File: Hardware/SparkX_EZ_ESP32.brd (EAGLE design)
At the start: 10.7 x 40.6 mm, 59 parts, among them Q1 MBT3904DW1T1, U1 3.3V, U2 ESP32, U3 W25QXX128MBIT-6X5, U4 CP210X, X1 32.768kHz, X2 40MHz

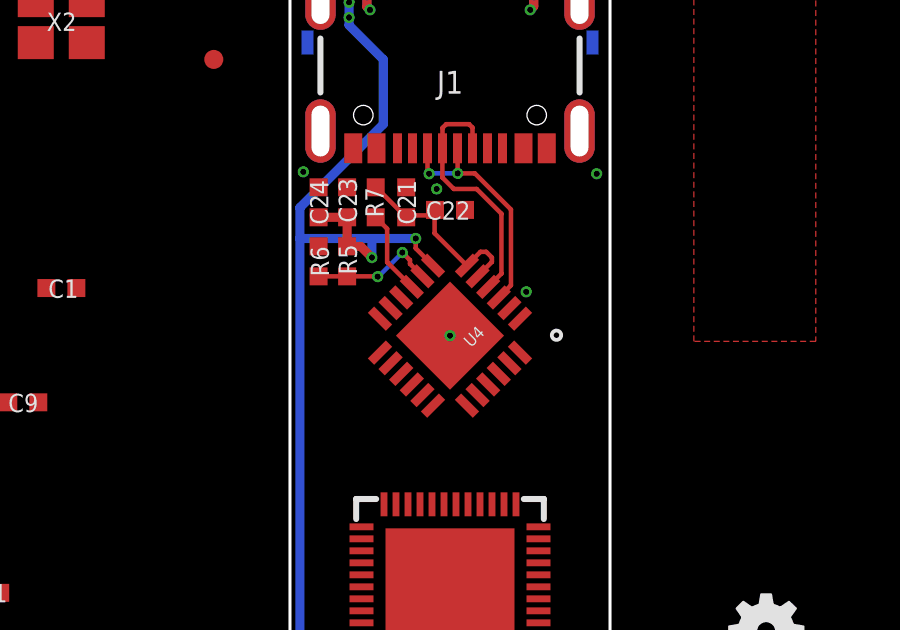
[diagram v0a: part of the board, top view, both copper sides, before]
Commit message: Add CP2102 package outline
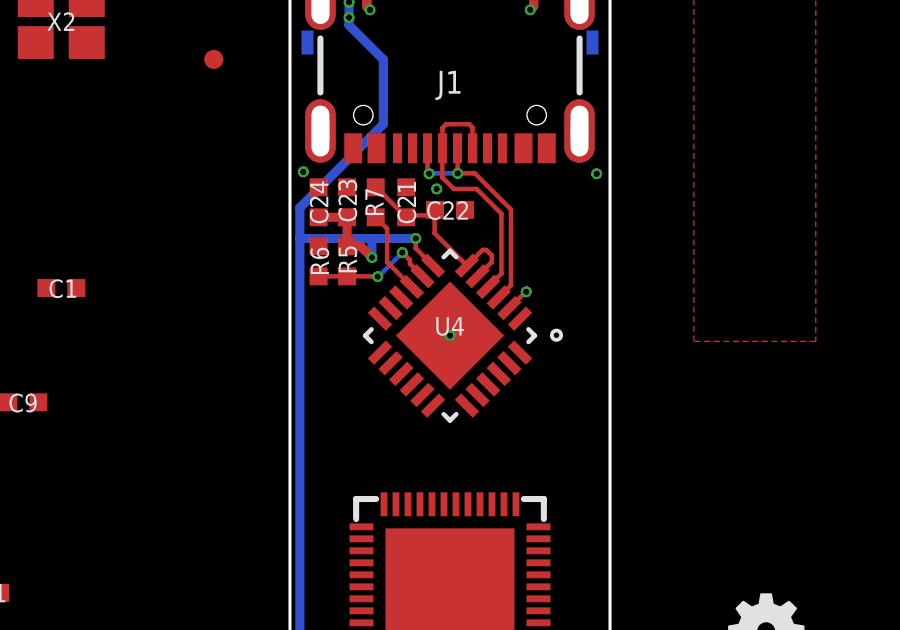
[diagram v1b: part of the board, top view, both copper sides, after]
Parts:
- A1: value (none) -> ANTENNA2.4GHZ-8.0X1.0MM
- U3: device SparkFun-MicroMod:WSON-8-6X5 -> SparkFun-IC-Memory:WSON-8-6X5
- U4: value CP210X -> CP2102N
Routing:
- net GND: track 7.88 -> 8.67 mm

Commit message: Routed
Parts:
- added !BOOT!, !RESET!, FLASH_VDD, RXT, TXT, USB_3V3: TEST-POINT3X4, SparkFun-Connectors:PAD.03X.04
- added U$10: (no value), output:#FVDD#0
- added U$2, U$3: (no value), output:EZ_ESP320
- added U$5: (no value), output:#TXT#0
- added U$6: (no value), output:#RXT#0
- added U$7: (no value), output:##BOOT##0
- added U$8: (no value), output:##RESET##0
- added U$9: (no value), output:#USB_3V3#0
- U3: value W25QXX128MBIT-6X5 -> W25QXX128MBIT-6X5-SKINNY_CENTER; device SparkFun-IC-Memory:WSON-8-6X5 -> SparkFun-IC-Memory:WSON-8-6X5-SKINNY_CENTERPAD
- moved U1 44.2 mm to (2.86, 5.14), flipped to the bottom, turned to 90 degrees
- moved C3 37.1 mm to (4.70, 19.4), flipped to the bottom, turned to 90 degrees
- moved Q1 35.8 mm to (6.35, 25.4), flipped to the bottom, turned to 270 degrees
- moved R10 35.4 mm to (8.64, 31.5), turned to 180 degrees
- moved C13 34.3 mm to (7.62, 23.9)
- moved C4 34.1 mm to (4.70, 17.4), flipped to the bottom, turned to 270 degrees
- moved C6 31.5 mm to (2.32, 22.5), turned to 270 degrees
- moved R1 31.2 mm to (1.78, 7.30), flipped to the bottom
- moved C7 30.4 mm to (2.32, 24.6), flipped to the bottom, turned to 270 degrees
- moved C15 30.0 mm to (9.81, 23.2), flipped to the bottom, turned to 90 degrees
- moved C2 29.4 mm to (5.40, 5.14), flipped to the bottom, turned to 90 degrees
- moved C1 27.8 mm to (1.78, 3.05), flipped to the bottom, turned to 180 degrees
- moved L1 26.2 mm to (2.32, 24.4), turned to 90 degrees
- moved R8 25.6 mm to (6.35, 27.2), flipped to the bottom
- moved R4 25.5 mm to (7.62, 23.0), turned to 180 degrees
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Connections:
- net 39-BATT/3 renamed N$3
- new net RXT: RXT.1, U4.13
- new net TXT: TXT.1, U4.14
- net !RESET: now also !RESET!.1
- net 0-!BOOT!: now also !BOOT!.1
- net FLASH_VDD: now also FLASH_VDD.1
- net USB_3V3: now also USB_3V3.1
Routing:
- net 3.3V: track 21.7 -> 125.6 mm, vias 6 -> 19
- net GND: track 8.67 -> 51.8 mm, vias 13 -> 47
- net SDA: track 41.7 -> 69.7 mm, vias 2 -> 3
- net SCL: track 41.5 -> 68.5 mm, vias 2 -> 3
- net 0-!BOOT!: track 0.00 -> 19.0 mm, vias 0 -> 2
- net CS1: track 42.0 -> 60.2 mm, vias 2 -> 3
- net FLASH_SDO: track 0.00 -> 14.9 mm
- net V_USB: track 53.2 -> 67.0 mm
- net FLASH_SCS: track 0.00 -> 13.1 mm
- net !RESET: track 0.00 -> 12.3 mm, vias 0 -> 1
- net PROC_PWR_EN: track 41.5 -> 53.6 mm, vias 2 -> 4
- net FLASH_SWP: track 0.00 -> 10.3 mm, vias 0 -> 2
- net FLASH_VDD: track 0.00 -> 9.47 mm, vias 0 -> 1
- net N$2: track 0.00 -> 9.26 mm, vias 0 -> 2
- net U0RXD: track 0.00 -> 9.14 mm
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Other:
- board text added: "JLCPCB JLC7628 4-Layer 1.6mm Impedance Control 4-Layer Board 1.6mm Thickness 1oz Copper (Outer layers) ENIG Finish When running the panelizer, add a vertical gap of 0.2" to make the boards easier to separate"
- board text removed: "JLCPCB JLC7628 4-Layer 0.8mm Impedance Control 4-Layer Board 0.8mm Thickness 1oz Copper (Outer layers) ENIG Finish When running the panelizer, add a vertical gap of 0.2" to make the boards easier to separate"

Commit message: Ready for review
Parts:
- moved C10 0.90 mm to (2.32, 23.4), turned to 270 degrees
- moved C7 0.89 mm to (2.32, 25.5), turned to 90 degrees
- moved C11 0.74 mm to (1.33, 21.3), turned to 270 degrees
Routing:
- net GND: track 51.8 -> 41.9 mm
- net 3: track 4.01 -> 2.72 mm
- net N$3: track 3.12 -> 2.02 mm
- net 6: track 3.41 -> 4.50 mm
- net RXT: track 3.79 -> 2.81 mm
- net V_USB: track 67.0 -> 67.8 mm
- net N$54: track 5.79 -> 5.26 mm

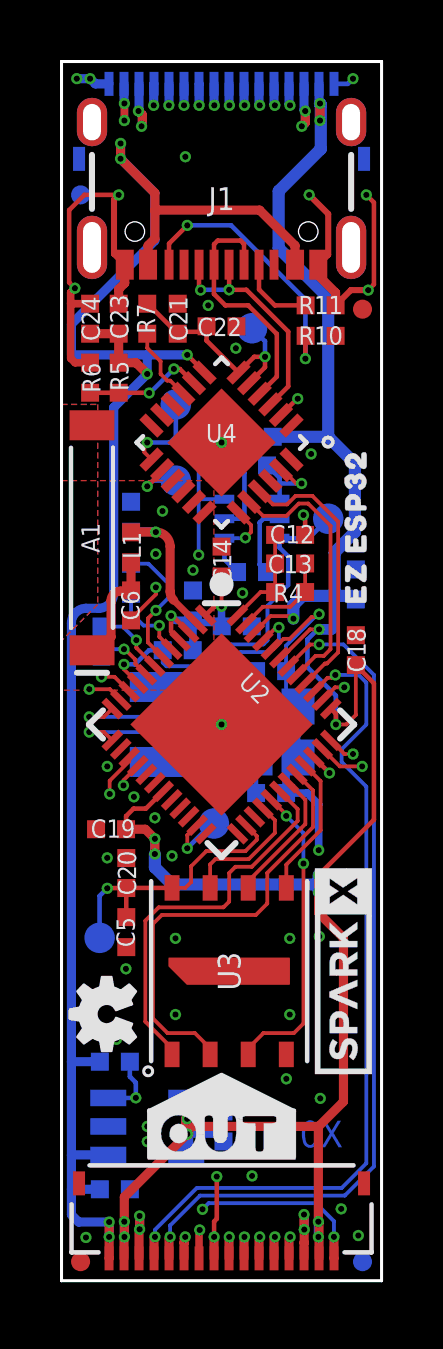
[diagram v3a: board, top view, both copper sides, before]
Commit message: Add neopixel. Add mirror-symmetric production panel
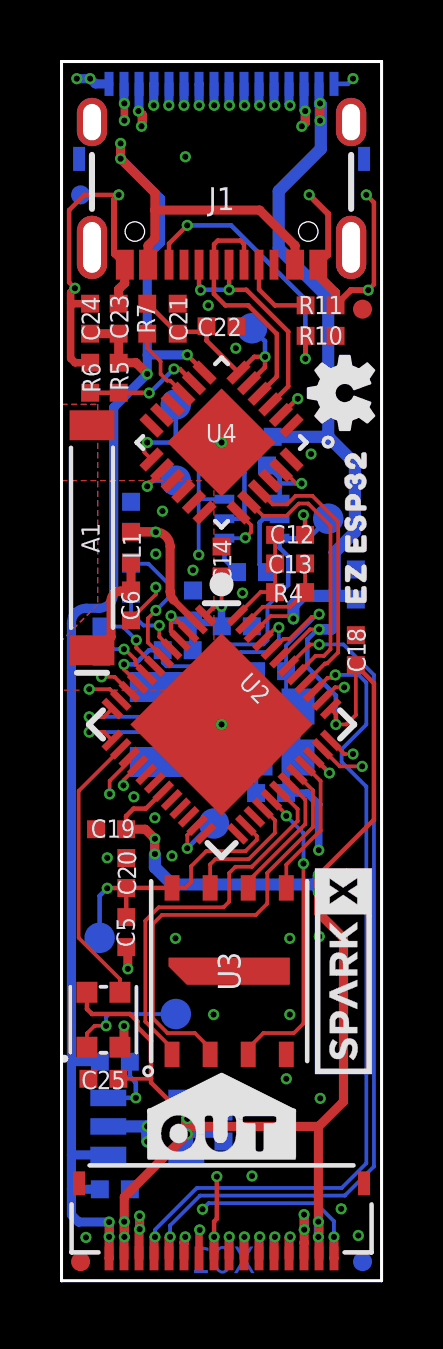
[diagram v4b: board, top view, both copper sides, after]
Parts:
- added C25: 0.1uF, SparkFun-Capacitors:0402-TIGHT
- added D1: WS2812_2020, SparkFun-LED:WS2812-2020
- added LED_DO: TEST-POINT3X4, SparkFun-Connectors:PAD.03X.04
- added LOGO4: SPECIAL_INSTRUCTIONS-PRODUCTION, SparkFun-Aesthetics:PRODUCTION_INSTRUCTIONS
- added U$11: (no value), output:#LED_DO#0
- U1: value 3.3V -> MIC5219 3.3V
- moved FRAME1 31.9 mm to (48.3, -41.9)
- moved LOGO2 22.2 mm to (9.43, 29.6)
- moved LOGO1 20.4 mm to (20.3, 71.1)
- moved LOGO3 4.80 mm to (8.26, 5.08)
- moved U$5 0.19 mm to (1.65, 26.9)
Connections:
- new net LED: D1.DI, U2.14
- new net N$4: D1.DO, LED_DO.1
- net 3.3V: now also C25.1, D1.VCC
- net GND: now also C25.2, D1.GND
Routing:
- net LED: track 0.00 -> 9.27 mm
- net 3.3V: track 125.6 -> 133.0 mm
- net N$4: track 0.00 -> 3.86 mm, vias 0 -> 1
- net V_USB: track 67.8 -> 64.4 mm
- net GND: track 41.9 -> 45.2 mm, vias 47 -> 46
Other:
- board text added: "JLCPCB JLC7628 4-Layer 1.2mm Impedance Control 4-Layer Board 1.2mm Thickness 1oz Copper (Outer layers) ENIG Finish When running the panelizer, add a vertical gap of 0.2" to make the boards easier to separate"
- board text added: "Populate the bottom layer components first to avoid problems placing the IN connector if the USB-C connector solder paste leaks out of the bottom of the routed holes"
- board text removed: "JLCPCB JLC7628 4-Layer 1.6mm Impedance Control 4-Layer Board 1.6mm Thickness 1oz Copper (Outer layers) ENIG Finish When running the panelizer, add a vertical gap of 0.2" to make the boards easier to separate"

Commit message: Post-review updates
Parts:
- C1: value 0.1uF -> 2.2uF
- moved C11 1.17 mm to (1.08, 20.2)
- moved C18 0.32 mm to (10.1, 20.8)
- moved C7 0.23 mm to (2.44, 25.3)
- moved C10 0.18 mm to (2.44, 23.3)
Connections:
- net CS1: now also U2.17; no longer U2.15
- net CS2: now also U2.20; no longer U2.16
- net GPIO0: now also U2.16; no longer U2.10
- net GPIO1: now also U2.15; no longer U2.11
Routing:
- net SDA: track 69.7 -> 50.0 mm
- net SCL: track 68.5 -> 50.2 mm, vias 3 -> 4
- net 3.3V: track 133.0 -> 130.7 mm
- net N$3: track 2.02 -> 3.27 mm
- net GPIO0: track 43.7 -> 44.9 mm
- net CS1: track 60.2 -> 59.3 mm
- net GND: vias 46 -> 48

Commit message: Gapless production panel
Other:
- board text added: "JLCPCB JLC7628 4-Layer 1.2mm Impedance Control 4-Layer Board 1.2mm Thickness 1oz Copper (Outer layers) ENIG Finish"
- board text removed: "JLCPCB JLC7628 4-Layer 1.2mm Impedance Control 4-Layer Board 1.2mm Thickness 1oz Copper (Outer layers) ENIG Finish When running the panelizer, add a vertical gap of 0.2" to make the boards easier to separate"
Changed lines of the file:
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@@
 <layers>
 <layer number="1" name="Top" color="4" fill="1" visible="yes" active="yes"/>
-<layer number="2" name="Route2" color="63" fill="1" visible="yes" active="yes"/>
-<layer number="15" name="Route15" color="23" fill="1" visible="yes" active="yes"/>
+<layer number="2" name="Route2" color="63" fill="1" visible="no" active="yes"/>
+<layer number="15" name="Route15" color="23" fill="1" visible="no" active="yes"/>
 <layer number="16" name="Bottom" color="1" fill="1" visible="yes" active="yes"/>
 <layer number="17" name="Pads" color="2" fill="1" visible="yes" active="yes"/>
@@
 <layer number="23" name="tOrigins" color="15" fill="1" visible="yes" active="yes"/>
 <layer number="24" name="bOrigins" color="15" fill="1" visible="yes" active="yes"/>
-<layer number="25" name="tNames" color="57" fill="1" visible="yes" active="yes"/>
-<layer number="26" name="bNames" color="57" fill="1" visible="yes" active="yes"/>
-<layer number="27" name="tValues" color="7" fill="1" visible="yes" active="yes"/>
-<layer number="28" name="bValues" color="7" fill="1" visible="yes" active="yes"/>
-<layer number="29" name="tStop" color="7" fill="3" visible="yes" active="yes"/>
-<layer number="30" name="bStop" color="7" fill="6" visible="yes" active="yes"/>
-<layer number="31" name="tCream" color="7" fill="4" visible="yes" active="yes"/>
-<layer number="32" name="bCream" color="7" fill="5" visible="yes" active="yes"/>
-<layer number="33" name="tFinish" color="6" fill="3" visible="yes" active="yes"/>
-<layer number="34" name="bFinish" color="6" fill="6" visible="yes" active="yes"/>
-<layer number="35" name="tGlue" color="7" fill="4" visible="yes" active="yes"/>
-<layer number="36" name="bGlue" color="7" fill="5" visible="yes" active="yes"/>
-<layer number="37" name="tTest" color="7" fill="1" visible="yes" active="yes"/>
-<layer number="38" name="bTest" color="7" fill="1" visible="yes" active="yes"/>
-<layer number="39" name="tKeepout" color="4" fill="11" visible="yes" active="yes"/>
-<layer number="40" name="bKeepout" color="1" fill="11" visible="yes" active="yes"/>
-<layer number="41" name="tRestrict" color="4" fill="10" visible="yes" active="yes"/>
-<layer number="42" name="bRestrict" color="1" fill="10" visible="yes" active="yes"/>
-<layer number="43" name="vRestrict" color="2" fill="10" visible="yes" active="yes"/>
-<layer number="44" name="Drills" color="7" fill="1" visible="yes" active="yes"/>
+<layer number="25" name="tNames" color="57" fill="1" visible="no" active="yes"/>
+<layer number="26" name="bNames" color="57" fill="1" visible="no" active="yes"/>
+<layer number="27" name="tValues" color="7" fill="1" visible="no" active="yes"/>
+<layer number="28" name="bValues" color="7" fill="1" visible="no" active="yes"/>
+<layer number="29" name="tStop" color="7" fill="3" visible="no" active="yes"/>
+<layer number="30" name="bStop" color="7" fill="6" visible="no" active="yes"/>
+<layer number="31" name="tCream" color="7" fill="4" visible="no" active="yes"/>
+<layer number="32" name="bCream" color="7" fill="5" visible="no" active="yes"/>
+<layer number="33" name="tFinish" color="6" fill="3" visible="no" active="yes"/>
+<layer number="34" name="bFinish" color="6" fill="6" visible="no" active="yes"/>
+<layer number="35" name="tGlue" color="7" fill="4" visible="no" active="yes"/>
+<layer number="36" name="bGlue" color="7" fill="5" visible="no" active="yes"/>
+<layer number="37" name="tTest" color="7" fill="1" visible="no" active="yes"/>
+<layer number="38" name="bTest" color="7" fill="1" visible="no" active="yes"/>
+<layer number="39" name="tKeepout" color="4" fill="11" visible="no" active="yes"/>
+<layer number="40" name="bKeepout" color="1" fill="11" visible="no" active="yes"/>
+<layer number="41" name="tRestrict" color="4" fill="10" visible="no" active="yes"/>
+<layer number="42" name="bRestrict" color="1" fill="10" visible="no" active="yes"/>
+<layer number="43" name="vRestrict" color="2" fill="10" visible="no" active="yes"/>
+<layer number="44" name="Drills" color="7" fill="1" visible="no" active="yes"/>
 <layer number="45" name="Holes" color="7" fill="1" visible="yes" active="yes"/>
-<layer number="46" name="Milling" color="3" fill="1" visible="yes" active="yes"/>
-<layer number="47" name="Measures" color="7" fill="1" visible="yes" active="yes"/>
-<layer number="48" name="Document" color="7" fill="1" visible="yes" active="yes"/>
-<layer number="49" name="Reference" color="7" fill="1" visible="yes" active="yes"/>
-<layer number="50" name="dxf" color="7" fill="1" visible="yes" active="yes"/>
+<layer number="46" name="Milling" color="3" fill="1" visible="no" active="yes"/>
+<layer number="47" name="Measures" color="7" fill="1" visible="no" active="yes"/>
+<layer number="48" name="Document" color="7" fill="1" visible="no" active="yes"/>
+<layer number="49" name="Reference" color="7" fill="1" visible="no" active="yes"/>
+<layer number="50" name="dxf" color="7" fill="1" visible="no" active="yes"/>
 <layer number="51" name="tDocu" color="6" fill="1" visible="yes" active="yes"/>
-<layer number="52" name="bDocu" color="7" fill="1" visible="yes" active="yes"/>
+<layer number="52" name="bDocu" color="7" fill="1" visible="no" active="yes"/>
 <layer number="3" name="Route3" color="17" fill="1" visible="no" active="no"/>
 <layer number="4" name="Route4" color="18" fill="1" visible="no" active="no"/>
@@
 1oz Copper (Outer layers)
 ENIG Finish
-When running the panelizer, add a vertical gap of 0.2"
-to make the boards easier to separate</text>
+</text>
 <dimension x1="0" y1="0" x2="10.668" y2="0" x3="5.334" y3="-3.81" textsize="1.778" textratio="15" layer="47" dtype="horizontal" unit="inch"/>
 <dimension x1="0" y1="40.64" x2="0" y2="0" x3="-3.810003125" y3="20.32" textsize="1.778" textratio="15" layer="47" dtype="vertical" unit="inch"/>

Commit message: Updates for JLCPCB manufacture
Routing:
- net CS0: track 43.0 -> 45.3 mm
- net SCL: track 50.2 -> 49.3 mm
- net CS1: track 59.3 -> 59.8 mm

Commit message: Update 16-way FPC Connector
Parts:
- IN, OUT: value FPC_16_0.5MM_BACKFLIP -> (none); device New_Parts_Connectors:FPC_16_DOUBLESIDED_BACKFLIP -> SparkFun-Connectors:FPC_16_0.5MM
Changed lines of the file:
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@@
 <element name="FD3" library="SparkFun-Aesthetics" package="FIDUCIAL-MICRO" value="FIDUCIALUFIDUCIAL" x="0.635" y="0.635" smashed="yes"/>
 <element name="FD4" library="SparkFun-Aesthetics" package="FIDUCIAL-MICRO" value="FIDUCIALUFIDUCIAL" x="10.033" y="0.635" smashed="yes" rot="MR0"/>
-<element name="IN" library="New_Parts_Connectors" package="FPC_16_DOUBLESIDED_BACKFLIP" value="FPC_16_0.5MM_BACKFLIP" x="5.334" y="38.5445" smashed="yes" rot="MR0">
-<attribute name="ATOM_PART" value="FPC05016-42201" x="5.334" y="38.5445" size="1.778" layer="28" font="vector" ratio="15" rot="MR0" display="off"/>
-<attribute name="PROD_ID" value="" x="5.334" y="38.5445" size="1.778" layer="28" font="vector" ratio="15" rot="MR0" display="off"/>
+<element name="IN" library="SparkFun-Connectors" package="FPC_16_0.5MM" value="" x="5.334" y="38.5445" smashed="yes" rot="MR0">
+<attribute name="PROD_ID" value="CONN-16066" x="5.334" y="38.5445" size="1.778" layer="28" font="vector" ratio="15" rot="MR0" display="off"/>
 </element>
-<element name="OUT" library="New_Parts_Connectors" package="FPC_16_DOUBLESIDED_BACKFLIP" value="FPC_16_0.5MM_BACKFLIP" x="5.334" y="2.0955" smashed="yes" rot="R180">
-<attribute name="ATOM_PART" value="FPC05016-42201" x="5.334" y="2.0955" size="1.778" layer="27" font="vector" ratio="15" rot="R180" display="off"/>
-<attribute name="PROD_ID" value="" x="5.334" y="2.0955" size="1.778" layer="27" font="vector" ratio="15" rot="R180" display="off"/>
+<element name="OUT" library="SparkFun-Connectors" package="FPC_16_0.5MM" value="" x="5.334" y="2.0955" smashed="yes" rot="R180">
+<attribute name="PROD_ID" value="CONN-16066" x="5.334" y="2.0955" size="1.778" layer="27" font="vector" ratio="15" rot="R180" display="off"/>
 </element>
 <element name="LOGO2" library="SparkFun-Aesthetics" package="OSHW-LOGO-MINI" value="OSHW-LOGOMINI" x="9.42975" y="29.591" smashed="yes" rot="R90"/>
